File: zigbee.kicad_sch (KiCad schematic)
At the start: 58 parts, among them J201 Conn_Coaxial, J203 TC2050, U201 SKY13317-373, U202 CC2652P1FRGZR, U203 CC2652P1FRGZR, X201 32.768kHz, X202 48MHz

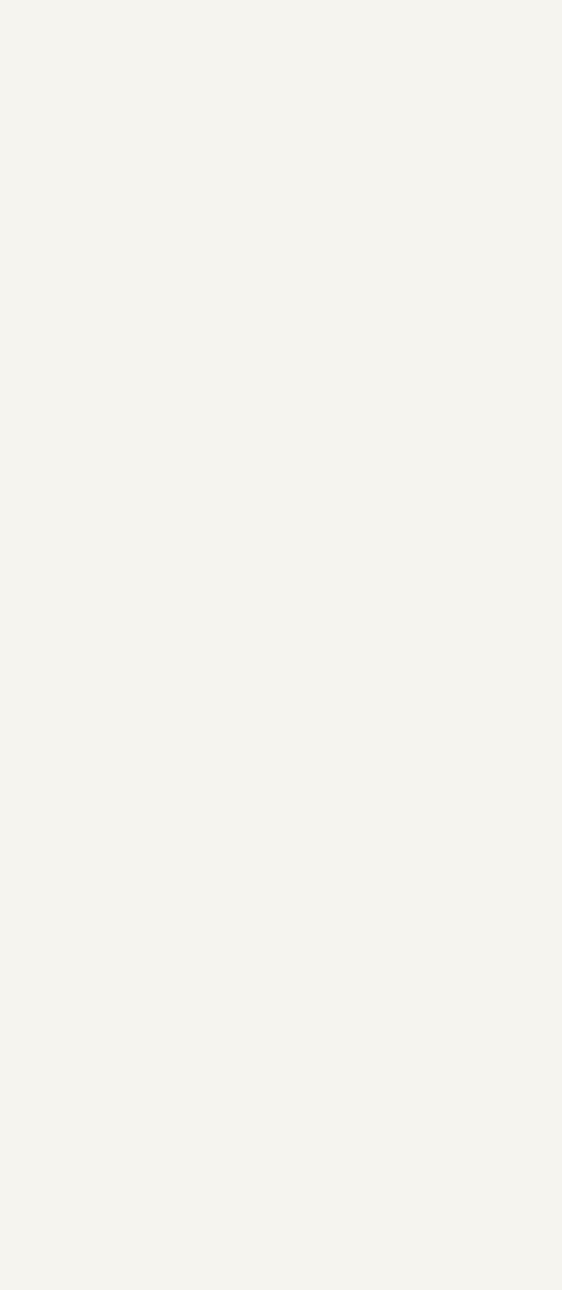
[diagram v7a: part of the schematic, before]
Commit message: Added CC2652PSIP schematic symbol. Switching out for CC2652P for RF simplicity
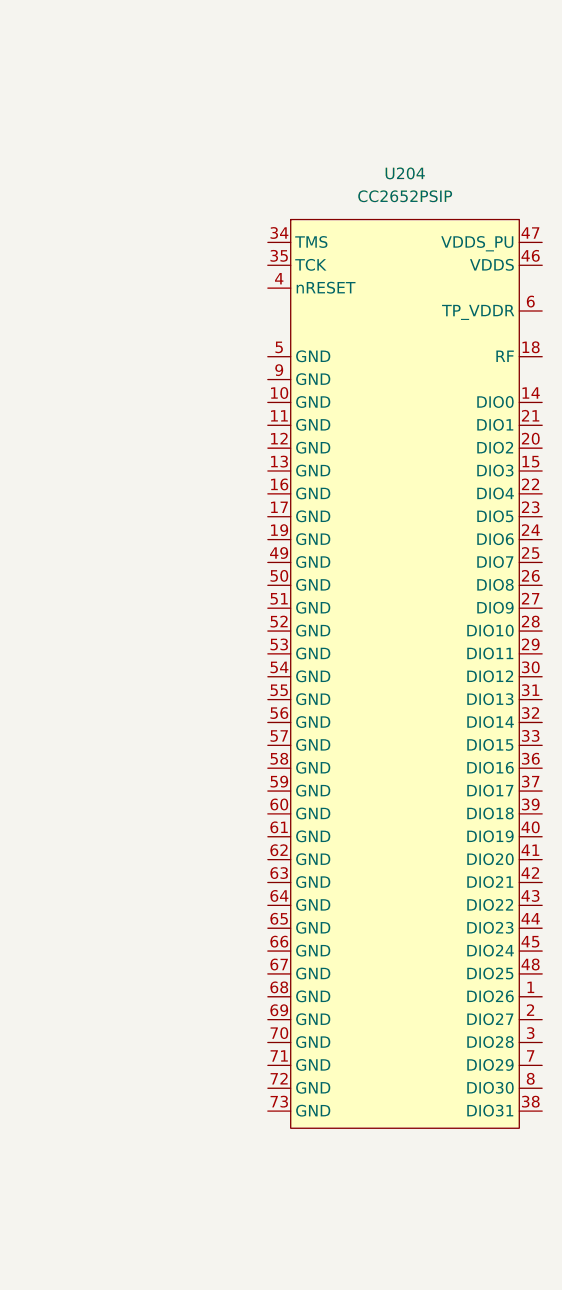
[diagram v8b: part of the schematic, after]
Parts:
- added U204: CC2652PSIP, symbol SoftServicesSymbolLibrary:CC2652PSIP
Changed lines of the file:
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@@
+	)
+	(symbol
+		(lib_id "SoftServicesSymbolLibrary:CC2652PSIP")
+		(at 509.27 148.59 0)
+		(unit 1)
+		(exclude_from_sim no)
+		(in_bom yes)
+		(on_board yes)
+		(dnp no)
+		(fields_autoplaced yes)
+		(property "Reference" "U204"
+			(at 509.27 109.22 0)
+			(effects
+				(font
+					(size 1.27 1.27)
+				)
+			)
+		)
+		(property "Value" "CC2652PSIP"
+			(at 509.27 111.76 0)
+			(effects
+				(font
+					(size 1.27 1.27)
+				)
+			)
+		)
+		(property "Footprint" ""
+			(at 509.27 148.59 0)
+			(effects
+				(font
+					(size 1.27 1.27)
+				)
+				(hide yes)
+			)
+		)
+		(property "Datasheet" ""
+			(at 509.27 148.59 0)
+			(effects
+				(font
+					(size 1.27 1.27)
+				)
+				(hide yes)
+			)
+		)
+		(property "Description" ""
+			(at 509.27 148.59 0)
+			(effects
+				(font
+					(size 1.27 1.27)
+				)
+				(hide yes)
+			)
+		)
+		(pin "10"
+		)
+		(pin "4"
+		)
+		(pin "19"
+		)
+		(pin "12"
+		)
+		(pin "52"
+		)
+		(pin "35"
+		)
+		(pin "60"
+		)
+		(pin "17"
+		)
+		(pin "59"
+		)
+		(pin "16"
+		)
+		(pin "11"
+		)
+		(pin "50"
+		)
+		(pin "9"
+		)
+		(pin "13"
+		)
+		(pin "56"
+		)
+		(pin "57"
+		)
+		(pin "53"
+		)
+		(pin "58"
+		)
+		(pin "34"
+		)
+		(pin "54"
+		)
+		(pin "55"
+		)
+		(pin "61"
+		)
+		(pin "49"
+		)
+		(pin "5"
+		)
+		(pin "51"
+		)
+		(pin "62"
+		)
+		(pin "63"
+		)
+		(pin "64"
+		)
+		(pin "65"
+		)
+		(pin "66"
+		)
+		(pin "67"
+		)
+		(pin "68"
+		)
+		(pin "69"
+		)
+		(pin "70"
+		)
+		(pin "71"
+		)
+		(pin "72"
+		)
+		(pin "73"
+		)
+		(pin "47"
+		)
+		(pin "46"
+		)
+		(pin "6"
+		)
+		(pin "18"
+		)
+		(pin "14"
+		)
+		(pin "21"
+		)
+		(pin "20"
+		)
+		(pin "15"
+		)
+		(pin "22"
+		)
+		(pin "23"
+		)
+		(pin "24"
+		)
+		(pin "25"
+		)
+		(pin "26"
+		)
+		(pin "27"
+		)
+		(pin "28"
+		)
+		(pin "29"
+		)
+		(pin "30"
+		)
+		(pin "31"
+		)
+		(pin "32"
+		)
+		(pin "33"
+		)
+		(pin "36"
+		)
+		(pin "37"
+		)
+		(pin "39"
+		)
+		(pin "40"
+		)
+		(pin "41"
+		)
+		(pin "42"
+		)
+		(pin "43"
+		)
+		(pin "44"
+		)
+		(pin "45"
+		)
+		(pin "48"
+		)
+		(pin "1"
+		)
+		(pin "2"
+		)
+		(pin "3"
+		)
+		(pin "7"
+		)
+		(pin "8"
+		)
+		(pin "38"
+		)
+		(instances
+			(project ""
+				(path "/b43b7bca-e50d-42ec-8ff0-e0016dfefe0a/4037e4ca-7763-453b-96d1-7d8342daaa99"
+					(reference "U204")
+					(unit 1)
+				)
+			)
+		)
 	)
 	(symbol
